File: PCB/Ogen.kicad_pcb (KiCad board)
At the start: 2 copper layers, 28 x 21.5 mm, 18 parts, among them J1 Input, U1 PMW3360DM-T2QU, U2 AP2127K-ADJ

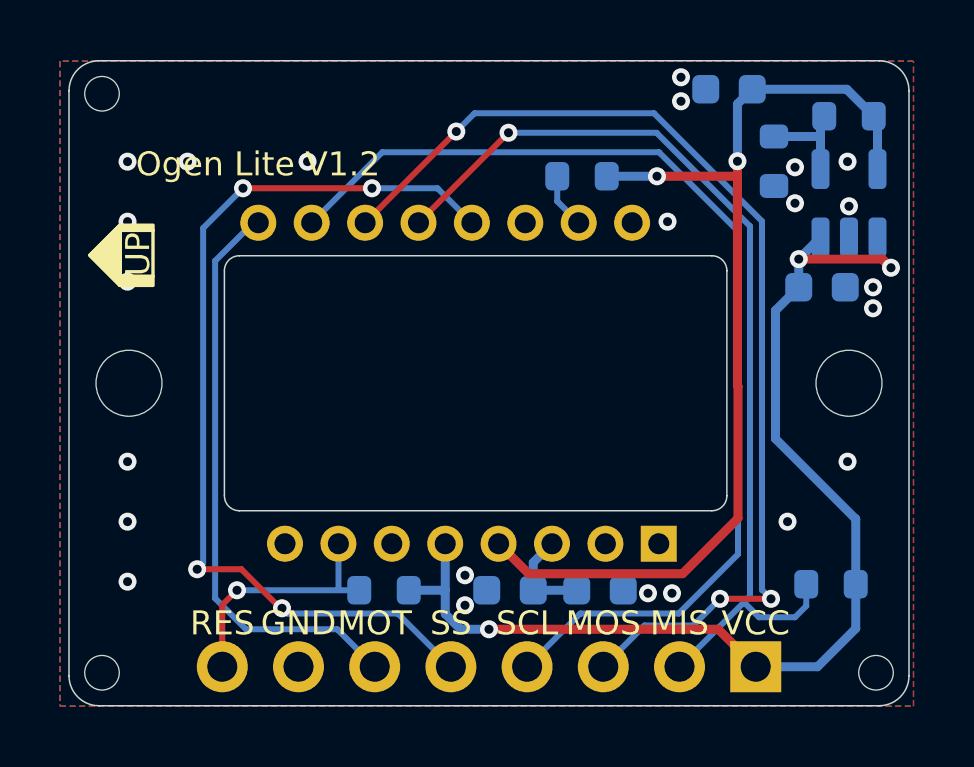
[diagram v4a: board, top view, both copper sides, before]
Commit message: V1.3 update
Changed LDO to XC6206P202MR.
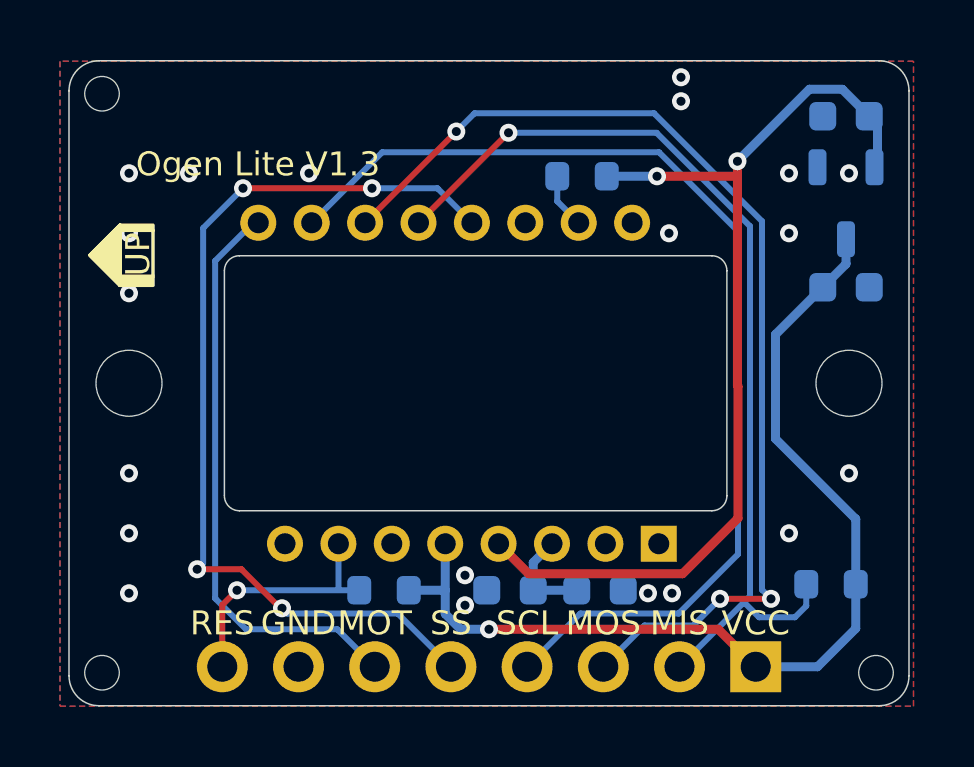
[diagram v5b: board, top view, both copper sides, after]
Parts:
- removed R4: 10k, Resistor_SMD:R_0603_1608Metric
- removed R5: 15k, Resistor_SMD:R_0603_1608Metric
- U2: value AP2127K-ADJ -> XC6206P202MR; footprint Package_TO_SOT_SMD:SOT-23-5 -> Ariamelon-Package:SOT-23-3
- moved C4 4.00 mm to (116.9, 56.1)
- moved C3 0.80 mm to (116.9, 61.8)
- moved U2 0.10 mm to (116.9, 59.0), turned to -90 degrees
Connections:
- U2 pad 1: +3V3 -> GND
- U2 pad 2: GND -> +2V
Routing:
- net +3V3: track 37.7 -> 33.6 mm, vias 3 -> 1
- net Net-(U2-ADJ): track 3.37 -> 0.00 mm
- net +2V: track 34.3 -> 32.8 mm
- net GND: vias 23 -> 20
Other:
- board text added: "Ogen Lite V1.3"
- board text removed: "Ogen Lite V1.2"
